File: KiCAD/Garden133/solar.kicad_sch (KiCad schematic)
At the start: 16 parts, among them Q1 FS8205A, Q2 AO3401A, U5 DW01A, U6 TP4056

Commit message: Board version 5
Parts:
- added Ca8: 100nF, Capacitor_SMD:C_0603_1608Metric_Pad1.08x0.95mm_HandSolder, symbol Device:C
- added F1: 0.5A, Diode_SMD:D_0805_2012Metric, symbol Device:Fuse_Small
- added Ru8: 10k, Resistor_SMD:R_0603_1608Metric, symbol Device:R
- Ca10: renamed from Cb1; value 10uF -> 100nF; footprint Capacitor_SMD:C_0805_2012Metric_Pad1.18x1.45mm_HandSolder -> Capacitor_SMD:C_0603_1608Metric_Pad1.08x0.95mm_HandSolder
- U5: symbol marbastlib-various:DW01A -> Battery_Management:DW01A
- U6: footprint Package_SO:SOIC-8-1EP_3.9x4.9mm_P1.27mm_EP2.29x3mm -> Package_SO:SOIC-8-1EP_3.9x4.9mm_P1.27mm_EP2.41x3.3mm_ThermalVias; symbol TP4056:TP4056 -> Battery_Management:TP4056-42-ESOP8
- renumbered Ca4 to Ca9, Cb4 to Cb2, R2 to R1, RPULL1 to R2u1, RL3 to Rl3
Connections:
- net +5V: now also F1.2; no longer D3.1 (K), Q2.2 (S)
- net GND: now also R2u1.1, U6.1 (TEMP), Ca8.1; no longer R2u1.2
- net VSOLAR+: now also Ru8.1; no longer R2u1.1
- new net: D3.1 (K), F1.1, Q2.2 (S)
- new net ADC1_CH7: Ca8.2, R2u1.2, Ru8.2
- no-connect marks 3 -> 2
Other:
- moved on the sheet: R2u1, RPROG1

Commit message: Update for board v6
- Added OpenSCAD models for Solar panel mount, tray for board+battery
- ADC Adjustment because using 220k resistors, not 200k.
- Licenses updated
- Remove support for v4 boards, update ADC slopes
- Board v6.0 (ordered)
- Support publishing more data via LoRa.
  Not able to include solar, due to packet size limitations.
- og3 version -> 0.3.10
- add raw_counts to packet
- add a filter for the moisture readings
- support normal mode -- deep sleep
  Normal mode is enabled based on the reading of the debug switch
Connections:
- net VBATTERY- is gone; now on net GND: Ca10.2, Q1.2, Q1.3, U5.6 (GND)
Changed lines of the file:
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@@
+		)
+	)
+	(text "VBAT-"
+		(exclude_from_sim no)
+		(at 49.022 107.95 0)
+		(effects
+			(font
+				(size 1.27 1.27)
+			)
 		)
 	)
@@
 				)
 				(justify left)
-				(hide yes)
-			)
-		)
-	)
-	(global_label "VBATTERY-"
-		(shape input)
-		(at 54.61 107.95 180)
-		(fields_autoplaced yes)
-		(effects
-			(font
-				(size 1.27 1.27)
-			)
-			(justify right)
-		)
-		(property "Intersheetrefs" "${INTERSHEET_REFS}"
-			(at 41.2418 107.95 0)
-			(effects
-				(font
-					(size 1.27 1.27)
-				)
-				(justify right)
 				(hide yes)
 			)
@@
 					(unit 1)
 				)
+			)
+		)
+	)
+	(symbol
+		(lib_id "power:GND")
+		(at 54.61 107.95 0)
+		(unit 1)
+		(exclude_from_sim no)
+		(in_bom yes)
+		(on_board yes)
+		(dnp no)
+		(fields_autoplaced yes)
+		(property "Reference" "#PWR049"
+			(at 54.61 114.3 0)
+			(effects
+				(font
+					(size 1.27 1.27)
+				)
+				(hide yes)
+			)
+		)
+		(property "Value" "GND"
+			(at 54.61 113.03 0)
+			(effects
+				(font
+					(size 1.27 1.27)
+				)
+			)
+		)
+		(property "Footprint" ""
+			(at 54.61 107.95 0)
+			(effects
+				(font
+					(size 1.27 1.27)
+				)
+				(hide yes)
+			)
+		)
+		(property "Datasheet" ""
+			(at 54.61 107.95 0)
+			(effects
+				(font
+					(size 1.27 1.27)
+				)
+				(hide yes)
+			)
+		)
+		(property "Description" "Power symbol creates a global label with name \"GND\" , ground"
+			(at 54.61 107.95 0)
+			(effects
+				(font
+					(size 1.27 1.27)
+				)
+				(hide yes)
+			)
+		)
+		(pin "1"
+		)
+		(instances
+			(project "Garden133"
+				(path "/f291efaa-4a5d-4b0c-9fc2-9a2012037d5f/68ad4c29-b646-4e97-9a96-445ccffd346c"
+					(reference "#PWR049")
+					(unit 1)
+				)

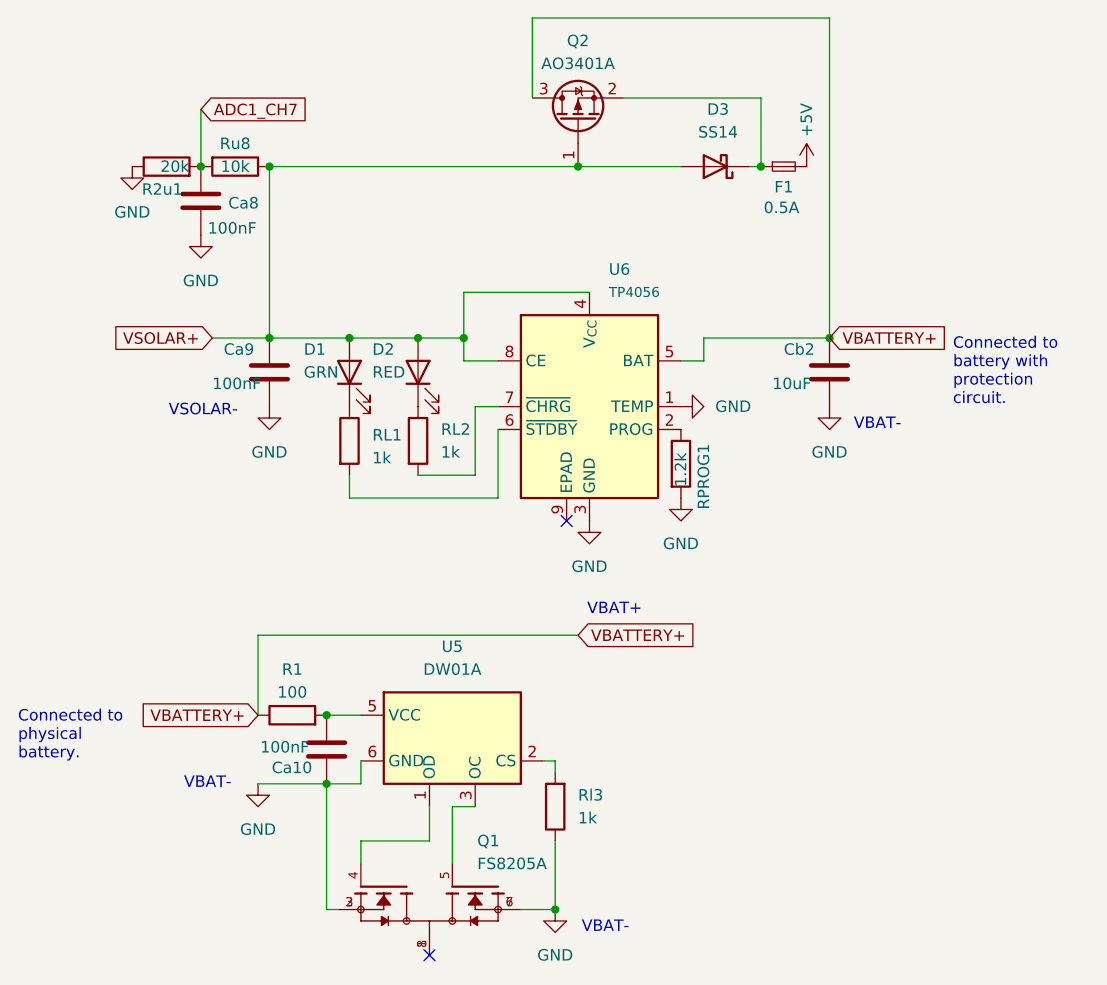
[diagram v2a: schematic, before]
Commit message: Update PCB
- Button controls power to 3.3V LDO
- DIO readings for STDBY and CHRG
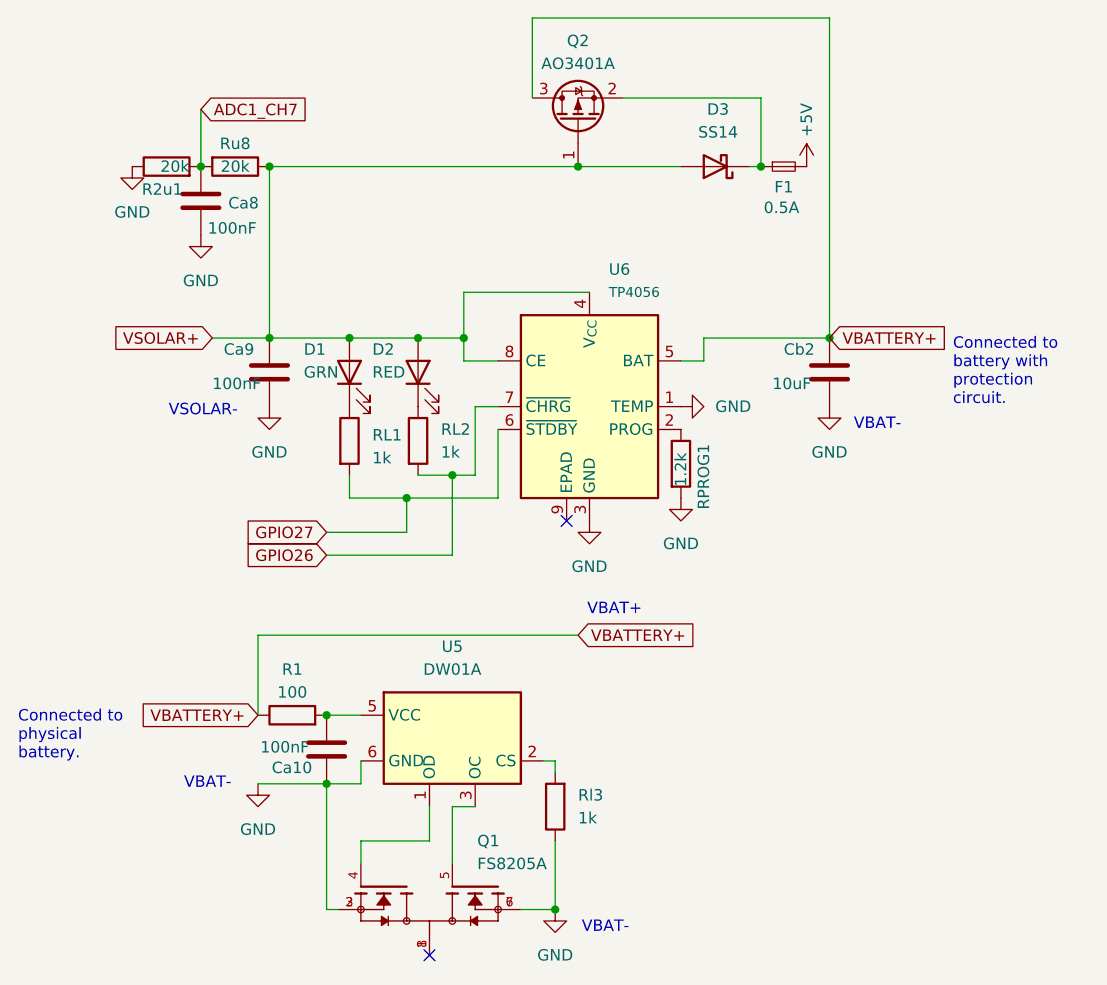
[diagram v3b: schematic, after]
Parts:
- Ru8: value 10k -> 20k
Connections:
- net GPIO27: now reaches RL1.2, U6.6 (~{STDBY})
- net GPIO26: now reaches RL2.2, U6.7 (~{CHRG})
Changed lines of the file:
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@@
+	)
+	(junction
+		(at 76.2 73.66)
+		(diameter 0)
+		(color 0 0 0 0)
 	)
 	(junction
@@
 		(color 0 0 0 0)
 	)
+	(junction
+		(at 71.12 76.2)
+		(diameter 0)
+		(color 0 0 0 0)
+	)
 	(no_connect
 		(at 73.66 127)
@@
 	(wire
 		(pts
-			(xy 64.77 76.2) (xy 81.28 76.2)
+			(xy 71.12 80.01) (xy 71.12 76.2)
+		)
+		(stroke
+			(width 0)
+			(type default)
+		)
+	)
+	(wire
+		(pts
+			(xy 64.77 76.2) (xy 71.12 76.2)
 		)
 		(stroke
@@
 	(wire
 		(pts
+			(xy 76.2 73.66) (xy 78.74 73.66)
+		)
+		(stroke
+			(width 0)
+			(type default)
+		)
+	)
+	(wire
+		(pts
 			(xy 77.47 53.34) (xy 77.47 58.42)
 		)
@@
 	(wire
 		(pts
+			(xy 62.23 82.55) (xy 76.2 82.55)
+		)
+		(stroke
+			(width 0)
+			(type default)
+		)
+	)
+	(wire
+		(pts
 			(xy 63.5 121.92) (xy 62.23 121.92)
 		)
@@
 	(wire
 		(pts
+			(xy 76.2 82.55) (xy 76.2 73.66)
+		)
+		(stroke
+			(width 0)
+			(type default)
+		)
+	)
+	(wire
+		(pts
+			(xy 62.23 80.01) (xy 71.12 80.01)
+		)
+		(stroke
+			(width 0)
+			(type default)
+		)
+	)
+	(wire
+		(pts
+			(xy 71.12 76.2) (xy 81.28 76.2)
+		)
+		(stroke
+			(width 0)
+			(type default)
+		)
+	)
+	(wire
+		(pts
 			(xy 54.61 107.95) (xy 62.23 107.95)
 		)
@@
 	(wire
 		(pts
-			(xy 72.39 73.66) (xy 78.74 73.66)
+			(xy 72.39 73.66) (xy 76.2 73.66)
 		)
 		(stroke
@@
 		)
 	)
+	(global_label "GPIO27"
+		(shape input)
+		(at 62.23 80.01 180)
+		(fields_autoplaced yes)
+		(effects
+			(font
+				(size 1.27 1.27)
+			)
+			(justify right)
+		)
+		(property "Intersheetrefs" "${INTERSHEET_REFS}"
+			(at 52.3505 80.01 0)
+			(effects
+				(font
+					(size 1.27 1.27)
+				)
+				(justify right)
+				(hide yes)
+			)
+		)
+	)
 	(global_label "VBATTERY+"
 		(shape input)
@@
 		)
 	)
+	(global_label "GPIO26"
+		(shape input)
+		(at 62.23 82.55 180)
+		(fields_autoplaced yes)
+		(effects
+			(font
+				(size 1.27 1.27)
+			)
+			(justify right)
+		)
+		(property "Intersheetrefs" "${INTERSHEET_REFS}"
+			(at 52.3505 82.55 0)
+			(effects
+				(font
+					(size 1.27 1.27)
+				)
+				(justify right)
+				(hide yes)
+			)
+		)
+	)
 	(symbol
 		(lib_id "Device:C")
@@
 			)
 		)
-		(property "Value" "10k"
+		(property "Value" "20k"
 			(at 52.07 39.37 90)
 			(effects

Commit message: Garden133 Board v6.2 (ordered from PCBWay)
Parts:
- D3: value SS14 -> UPS115UE3/TR7; footprint Diode_SMD:D_2010_5025Metric -> chl33_library:DO-216
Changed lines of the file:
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@@
 			)
 		)
-		(property "Value" "SS14"
+		(property "Value" "UPS115UE3/TR7"
 			(at 105.7275 35.56 0)
 			(effects
@@
 			)
 		)
-		(property "Footprint" "Diode_SMD:D_2010_5025Metric"
+		(property "Footprint" "chl33_library:DO-216"
 			(at 105.41 34.925 0)
 			(effects

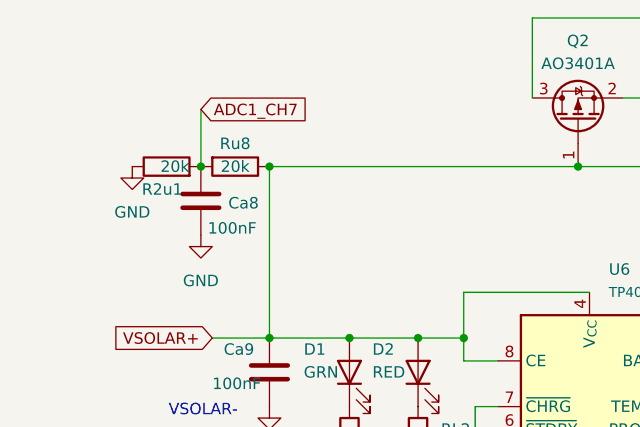
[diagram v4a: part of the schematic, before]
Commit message: update for board v6.2 (#1)
- Fix 20k resistor
- Board v6.2 update: standby/charge detection
-Maybe also fix hourly update?
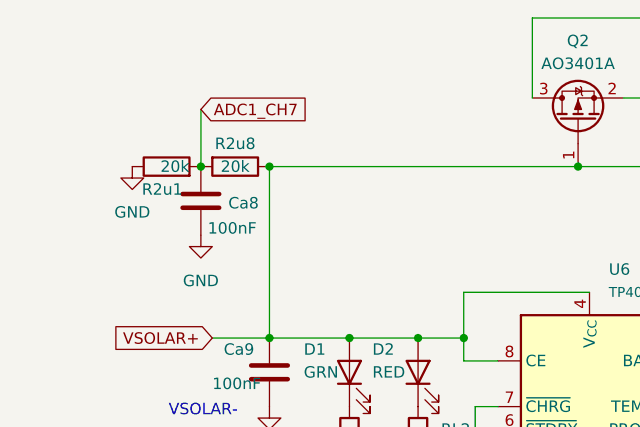
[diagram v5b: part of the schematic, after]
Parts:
- renumbered Ru8 to R2u8
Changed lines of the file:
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@@
 		(on_board yes)
 		(dnp no)
-		(property "Reference" "Ru8"
+		(property "Reference" "R2u8"
 			(at 52.07 36.83 90)
 			(effects
@@
 			(project "Garden133"
 				(path "/f291efaa-4a5d-4b0c-9fc2-9a2012037d5f/68ad4c29-b646-4e97-9a96-445ccffd346c"
-					(reference "Ru8")
+					(reference "R2u8")
 					(unit 1)
 				)
